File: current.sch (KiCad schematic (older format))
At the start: 42 parts

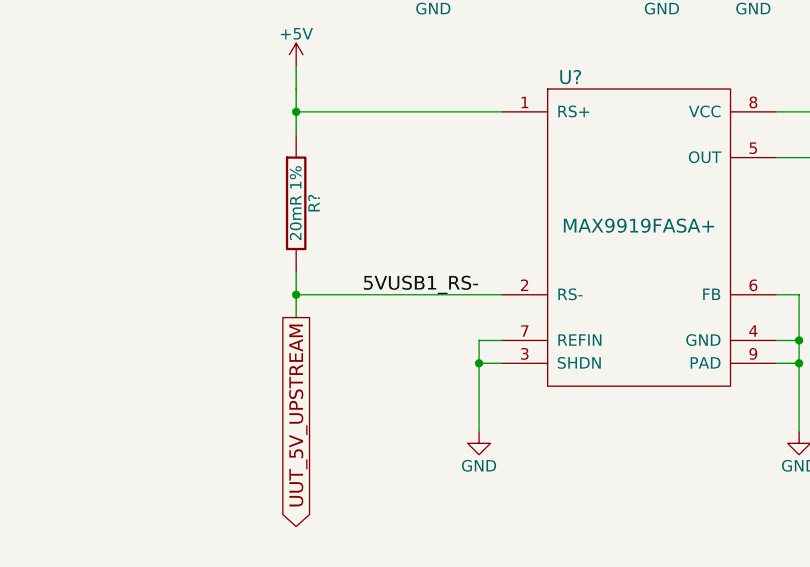
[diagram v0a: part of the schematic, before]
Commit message: added testpoint part number, small net naming changes
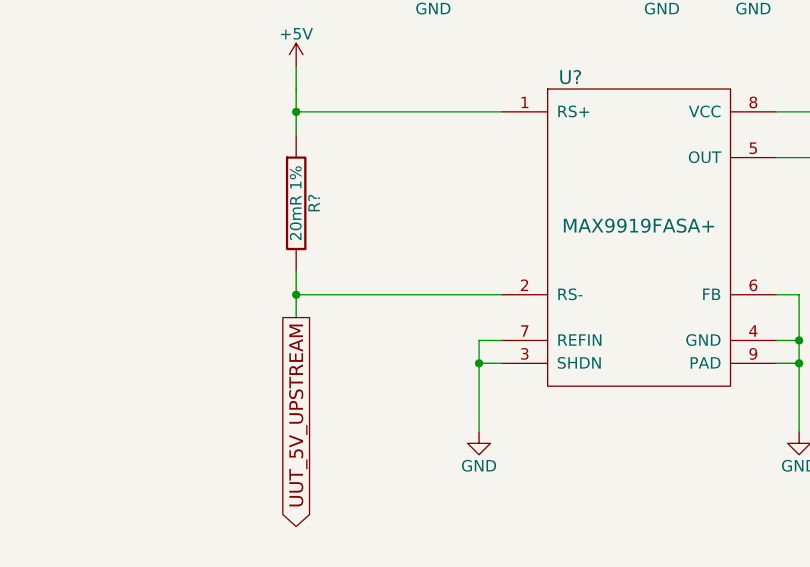
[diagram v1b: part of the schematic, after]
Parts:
- TP? (x4): value TP -> 0914-0-15-20-77-14-11-0
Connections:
- net UUT_5V_UPSTREAM: no longer Q?.3 (D), R?.2, U?.2 (RS-)
- new net 5VUSB1_RS-: Q?.3 (D), R?.2, U?.2 (RS-)
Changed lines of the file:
@@
 P 2600 2700
 F 0 "TP?" H 2600 2750 60  0000 C CNN
-F 1 "TP" H 2600 2650 60  0001 C CNN
+F 1 "0914-0-15-20-77-14-11-0" H 2600 2650 60  0001 C CNN
 F 2 "" H 2600 2700 60  0000 C CNN
 F 3 "" H 2600 2700 60  0000 C CNN
@@
 P 7900 2700
 F 0 "TP?" H 7900 2750 60  0000 C CNN
-F 1 "TP" H 7900 2650 60  0001 C CNN
+F 1 "0914-0-15-20-77-14-11-0" H 7900 2650 60  0001 C CNN
 F 2 "" H 7900 2700 60  0000 C CNN
 F 3 "" H 7900 2700 60  0000 C CNN
@@
 P 7900 6700
 F 0 "TP?" H 7900 6750 60  0000 C CNN
-F 1 "TP" H 7900 6650 60  0001 C CNN
+F 1 "0914-0-15-20-77-14-11-0" H 7900 6650 60  0001 C CNN
 F 2 "" H 7900 6700 60  0000 C CNN
 F 3 "" H 7900 6700 60  0000 C CNN
@@
 P 2600 6700
 F 0 "TP?" H 2600 6750 60  0000 C CNN
-F 1 "TP" H 2600 6650 60  0001 C CNN
+F 1 "0914-0-15-20-77-14-11-0" H 2600 6650 60  0001 C CNN
 F 2 "" H 2600 6700 60  0000 C CNN
 F 3 "" H 2600 6700 60  0000 C CNN
@@
 Text GLabel 13100 3900 3    60   Output ~ 0
 UUT_5V_UPSTREAM
-Text Label 13900 3800 2    60   ~ 0
-5VUSB1_RS-
 Text Label 15500 2900 1    60   ~ 0
 VCC_CSA_UUT

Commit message: annotated
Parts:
- gave numbers to parts that had none: 42

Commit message: components and footprints
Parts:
- C401, C402, C403, C404, C405, C406, C407, C408, C409, C410, C411, C412, C413, C414, C415: footprint (none) -> tm-kicad-lib:SMD-0402-C
- L401, L402, L403, L404, L405: footprint (none) -> tm-kicad-lib:SMD-0603-R
- Q401, Q402, Q403, Q404: footprint (none) -> Housings_SOT-23_SOT-143_TSOT-6:SOT-23
- R401, R402, R405, R406: footprint (none) -> tm-kicad-lib:SMD-0402-R
- R403, R404, R407, R408, R409: footprint (none) -> Resistors_SMD:R_1206
- TP401, TP402, TP403, TP404: value 0914-0-15-20-77-14-11-0 -> 0932-0-15-20-77-14-11-0
- U401, U402, U403, U404, U405: footprint (none) -> SMD_Packages:SOIC-8-N

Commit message: swapped testpoints
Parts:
- TP401, TP402, TP403, TP404: footprint (none) -> tm-kicad-lib:0932-0-15-20-77-14-11-0
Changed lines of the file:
@@
 F 0 "TP401" H 2600 2750 60  0000 C CNN
 F 1 "0932-0-15-20-77-14-11-0" H 2600 2650 60  0001 C CNN
-F 2 "" H 2600 2700 60  0001 C CNN
+F 2 "tm-kicad-lib:0932-0-15-20-77-14-11-0" H 2600 2700 60  0001 C CNN
 F 3 "" H 2600 2700 60  0000 C CNN
 	1    2600 2700
@@
 F 0 "TP403" H 7900 2750 60  0000 C CNN
 F 1 "0932-0-15-20-77-14-11-0" H 7900 2650 60  0001 C CNN
-F 2 "" H 7900 2700 60  0001 C CNN
+F 2 "tm-kicad-lib:0932-0-15-20-77-14-11-0" H 7900 2700 60  0001 C CNN
 F 3 "" H 7900 2700 60  0000 C CNN
 	1    7900 2700
@@
 F 0 "TP404" H 7900 6750 60  0000 C CNN
 F 1 "0932-0-15-20-77-14-11-0" H 7900 6650 60  0001 C CNN
-F 2 "" H 7900 6700 60  0001 C CNN
+F 2 "tm-kicad-lib:0932-0-15-20-77-14-11-0" H 7900 6700 60  0001 C CNN
 F 3 "" H 7900 6700 60  0000 C CNN
 	1    7900 6700
@@
 F 0 "TP402" H 2600 6750 60  0000 C CNN
 F 1 "0932-0-15-20-77-14-11-0" H 2600 6650 60  0001 C CNN
-F 2 "" H 2600 6700 60  0001 C CNN
+F 2 "tm-kicad-lib:0932-0-15-20-77-14-11-0" H 2600 6700 60  0001 C CNN
 F 3 "" H 2600 6700 60  0000 C CNN
 	1    2600 6700
